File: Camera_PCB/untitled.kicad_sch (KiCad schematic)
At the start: 22 parts

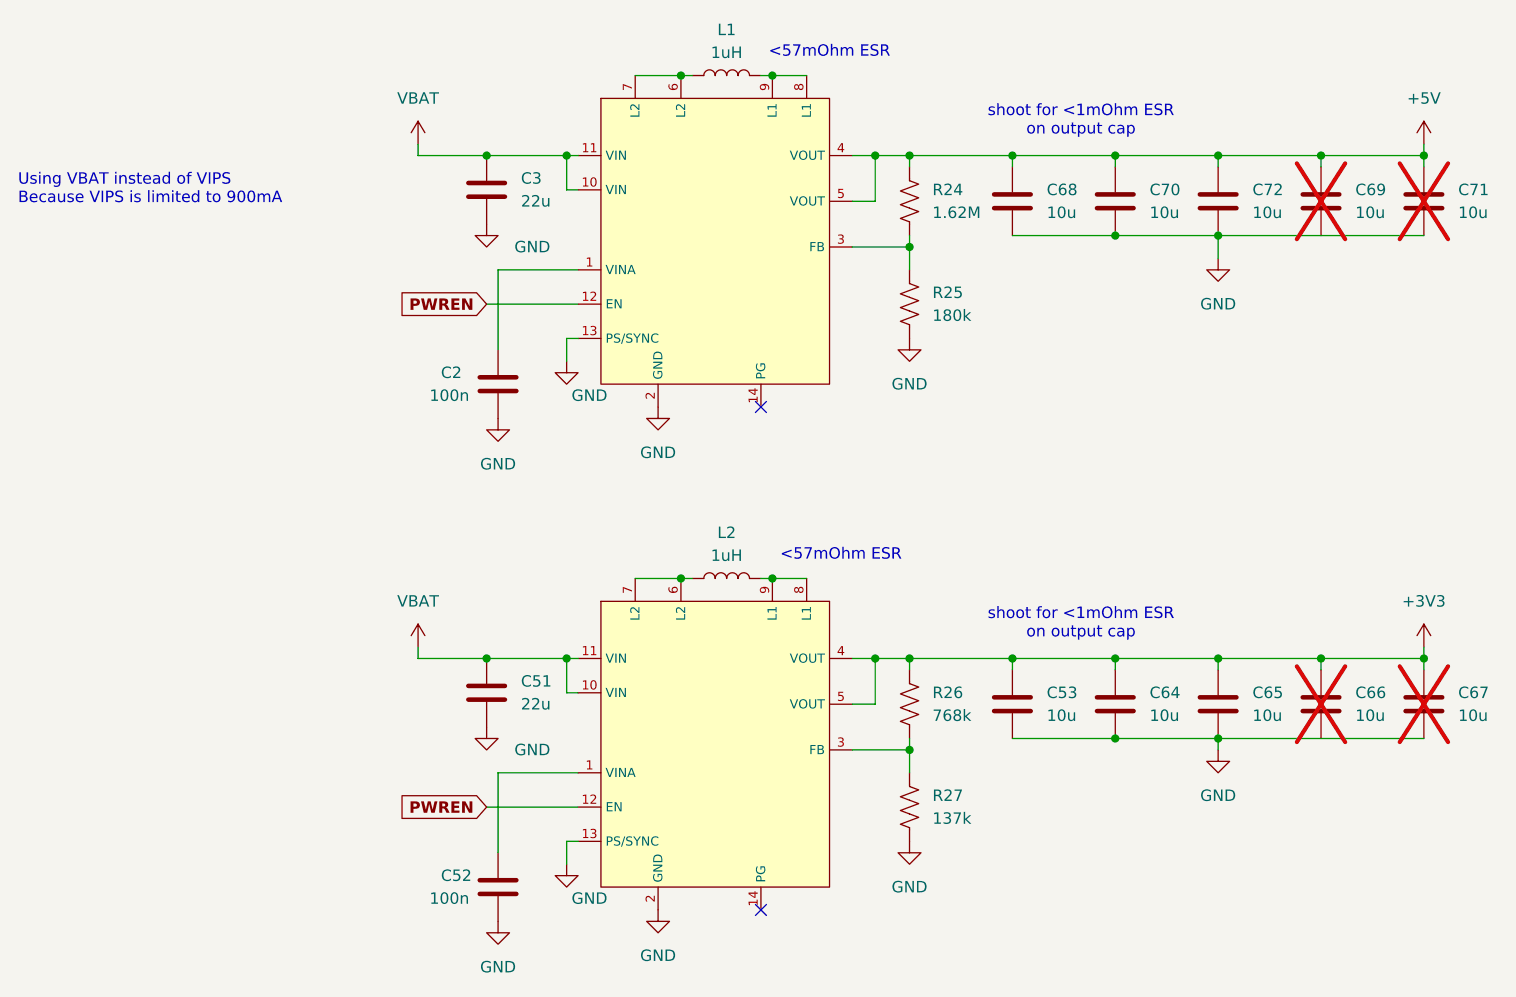
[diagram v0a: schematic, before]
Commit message: Schematic done, thoroughly reviewed by Jack, should get reviewed by Connor if possible.
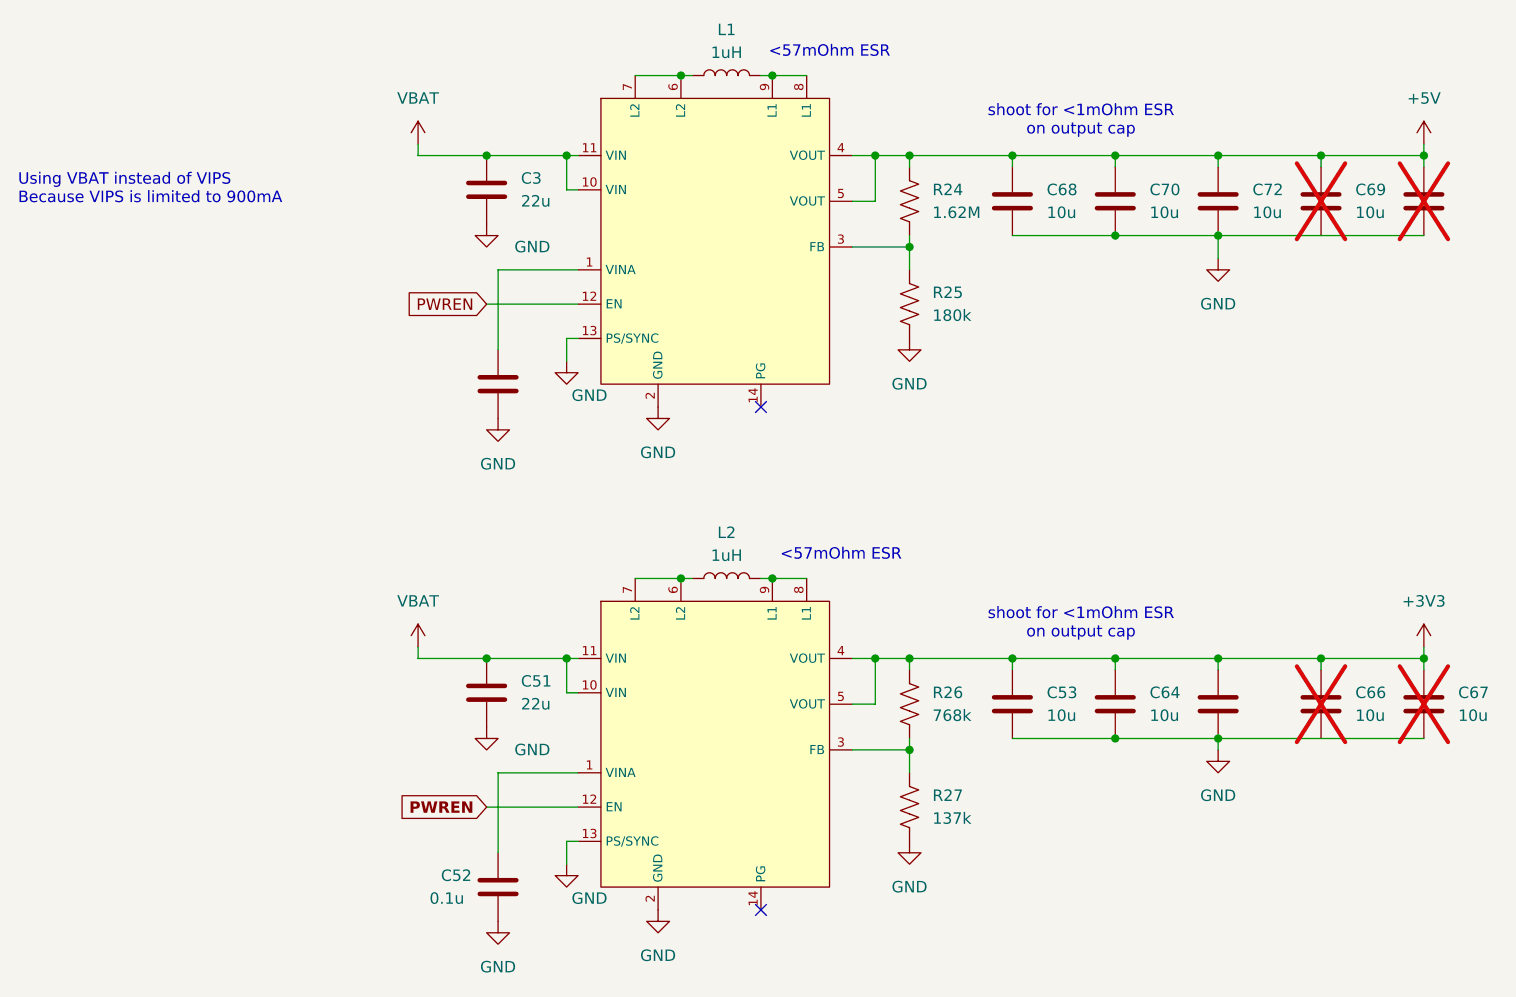
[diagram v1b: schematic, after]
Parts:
- C2, C52: value 100n -> 0.1u; DPN (none) -> GRM188R72A104KA35D; Distributor (none) -> DigiKey
- C3, C51: DPN (none) -> GRM21BZ71A226ME15L; Distributor (none) -> DigiKey
- C53, C64, C65, C66, C67, C68, C69, C70, C71, C72: DPN (none) -> GRM21BZ71E106KE15L; Distributor (none) -> DigiKey
- L1, L2: footprint (none) -> Inductor_SMD:L_Murata_DFE201610P; DPN (none) -> DFE201610E-1R0M=P2; Distributor (none) -> DigiKey
- R24: footprint (none) -> Resistor_SMD:R_0603_1608Metric_Pad0.98x0.95mm_HandSolder; DPN (none) -> RC0603FR-071M62L; Distributor (none) -> DigiKey
- R25: footprint (none) -> Resistor_SMD:R_0603_1608Metric_Pad0.98x0.95mm_HandSolder; DPN (none) -> RC0603FR-10180KL; Distributor (none) -> DigiKey
- R26: footprint (none) -> Resistor_SMD:R_0603_1608Metric_Pad0.98x0.95mm_HandSolder; DPN (none) -> RC0603FR-07768KL; Distributor (none) -> DigiKey
- R27: footprint (none) -> Resistor_SMD:R_0603_1608Metric_Pad0.98x0.95mm_HandSolder; DPN (none) -> RC0603FR-07137KL; Distributor (none) -> DigiKey
- TPS63020, TPS63021: Distributor Digikey -> DigiKey
